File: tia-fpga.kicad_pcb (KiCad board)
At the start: 2 copper layers, 76 x 36 mm, 28 parts, among them J1 PinSocket_1x24_P2.54mm_Vertic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, J2 PinHeader_1x20_P2.54mm_Vertic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, J3 PinHeader_1x20_P2.54mm_Vertic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, J4 PinSocket_1x24_P2.54mm_Vertic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, U1 SOIC-14_3.9x8.7mm_P1.27mm, U2 SOIC-20W_7.5x12.8mm_P1.27mm, U3 SOIC-20W_7.5x12.8mm_P1.27mm, U4 SOIC-20W_7.5x12.8mm_P1.27mm, U5 SOT-23-5

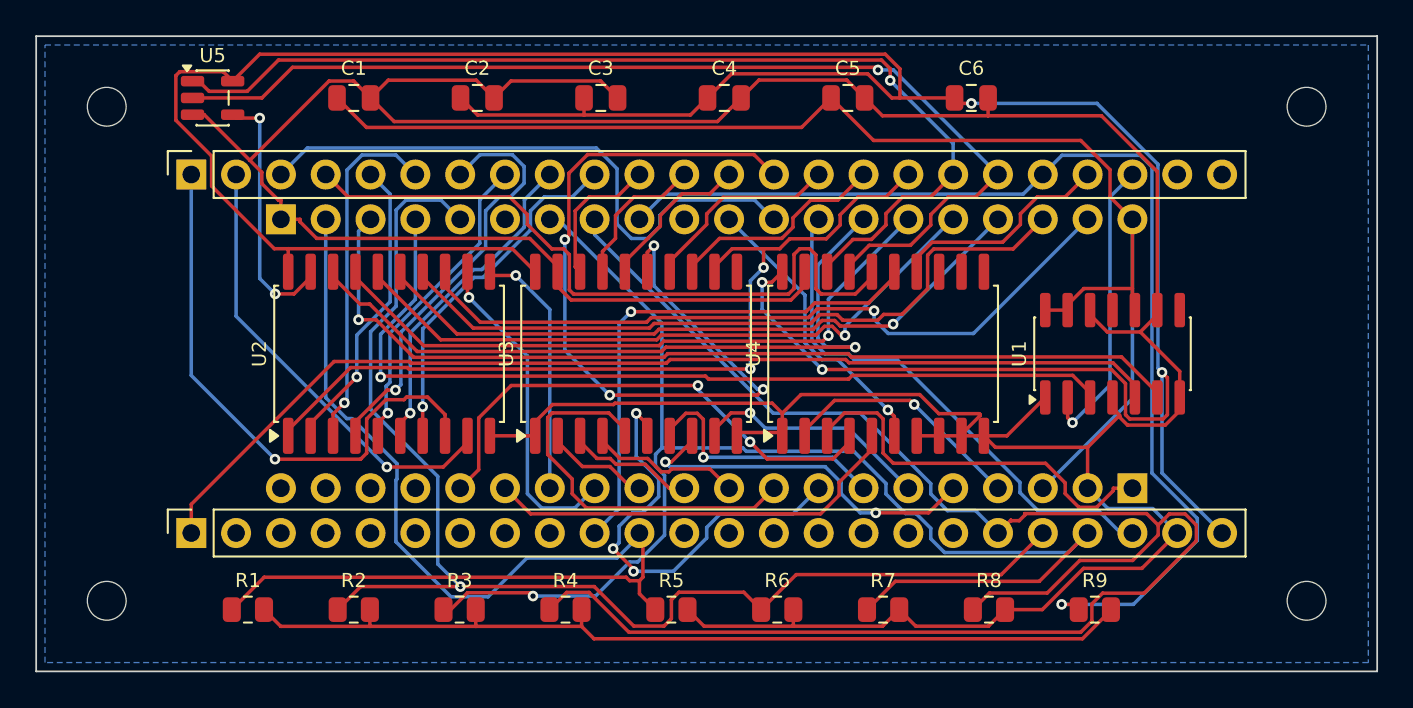
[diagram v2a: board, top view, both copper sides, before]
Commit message: Solve the pin assignment and reorder the buffers; drop the mounting holes
The buses crossed the board because the FPGA signals were assigned to
header positions in listing order. But which GPIO carries which signal is
free - the Tang Nano's header-to-package map is fixed, nothing says F_D0
has to sit on header pin 5. So it is now solved rather than listed:
Hungarian assignment over the 29 usable positions, minimising the
distance from each FPGA pin to the TIA pin it serves.

Summed |x_header - x_TIA| goes from 737 mm to 127 mm, with several
signals landing at exactly the same x as their target. The buffers are
then ordered by the centroid of what each carries: U1, U4, U3, U2.

Together:

  segments  758 -> 601
  vias       47 -> 31
  copper   2.19 -> 1.68 m

Mounting holes dropped. They were only ever going to hold the board to
something that does not exist inside a 2600 - it hangs from its own pins
in the TIA socket - and they had pushed the outline out to 76 x 36 mm.
Back to 70 x 32.

Silkscreen references moved beside the passives rather than above them;
in a 5 mm margin, above means into the board edge. That took the
silkscreen violations from 11 to 1.

Routing needed 0.18 mm track on top of the 0.13 mm clearance to close.
Worth recording how brittle this is: moving U5 by half a millimetre to
clear a courtyard warning cost two unrouted connections and a worse
score, because Freerouting is deterministic per input and any change
reshuffles everything. U5 went back where it was.

DRC: 0 clearance, 0 unconnected, 0 shorts. Two notes remain, both checked
by hand - one silk mark over copper, and the U5/J1 courtyard overlap
where the copper actually clears by 1.24 mm.

fpga/tia_fpga.cst carries the solved assignment and says not to reshuffle
it casually, since the layout depends on it.

Co-Authored-By: Claude Opus 5 <noreply@anthropic.com>
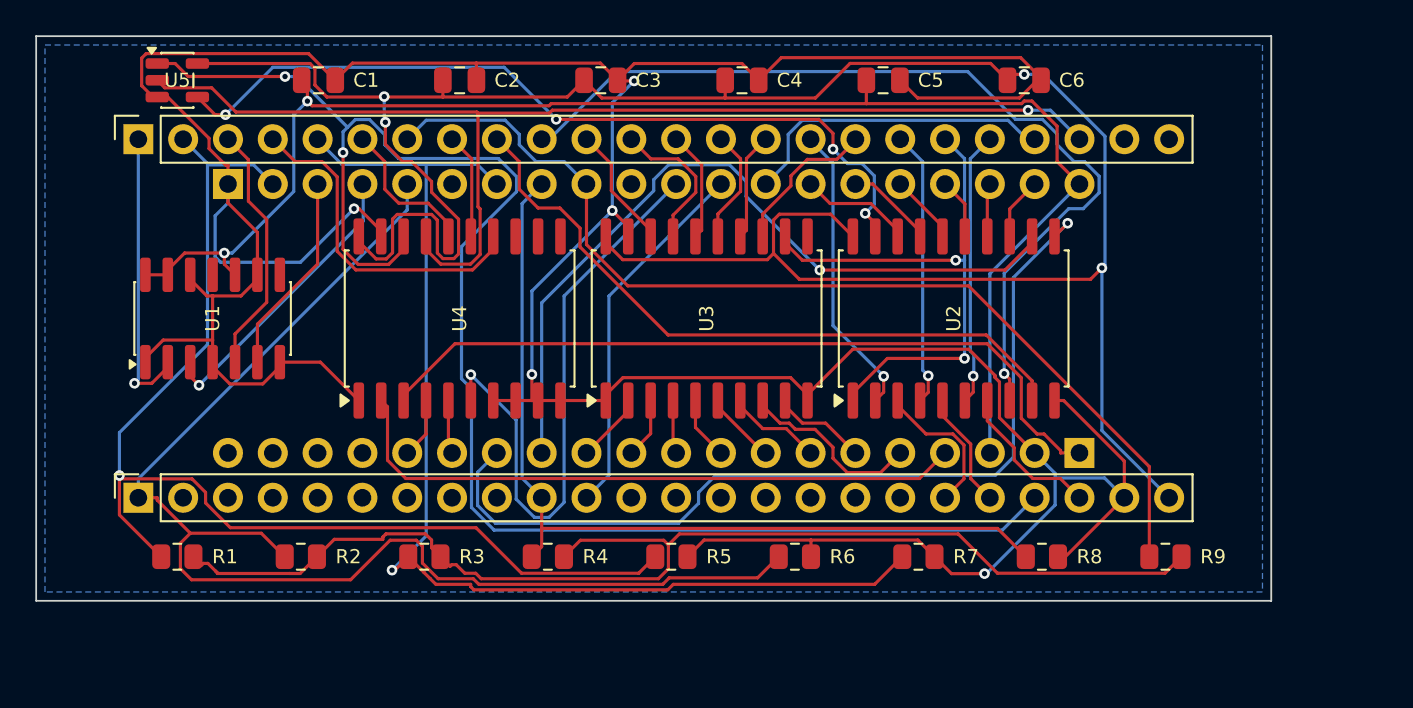
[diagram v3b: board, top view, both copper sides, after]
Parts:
- removed H1, H2, H3, H4: MountingHole_2.2mm_M2, MountingHole_2.2mm_M2
- moved U1 51.0 mm to (10.0, 16.0)
- moved U2 32.1 mm to (52.0, 16.0)
- moved U4 24.1 mm to (24.0, 16.0)
- moved R1 5.00 mm to (8.00, 29.5)
- moved R9 5.00 mm to (64.0, 29.5)
- moved U3 4.47 mm to (38.0, 16.0)
- moved R2 4.24 mm to (15.0, 29.5)
- moved R8 4.24 mm to (57.0, 29.5)
- moved J2 3.61 mm to (10.9, 8.38)
- moved J3 3.61 mm to (59.1, 23.6)
- moved R3 3.61 mm to (22.0, 29.5)
- moved R7 3.61 mm to (50.0, 29.5)
- moved J1 3.61 mm to (5.79, 5.84)
- moved J4 3.61 mm to (5.79, 26.2)
- moved C6 3.16 mm to (56.0, 2.50)
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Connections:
- J1 pad 1: /F_D6 -> /F_PHI0
- J1 pad 10: /F_D5 -> /F_D6
- J1 pad 16: /F_A5 -> /F_D0
- J1 pad 17: /F_RW -> /F_A5
- J1 pad 18: /F_CS0_N -> /F_D2
- J1 pad 19: /F_CS3_N -> /F_RW
- J1 pad 2: /F_D7 -> /F_CSYNC
- J1 pad 20: /F_COL -> /F_D4
- J1 pad 21: /F_OSC -> /F_AU0
- J1 pad 22: /F_PHI0 -> /F_CS3_N
- J1 pad 3: /F_AU1 -> /F_RDY
- J1 pad 4: /F_I4 -> /F_OSC
- J1 pad 5: /F_D0 -> /F_LUM2
- J1 pad 6: /F_D1 -> /F_I4
- J1 pad 7: /F_D2 -> /F_COL
- J1 pad 8: /F_D3 -> /F_I5
- J1 pad 9: /F_D4 -> /F_D7
- J4 pad 1: /F_RDY -> /F_LUM1
- J4 pad 10: /F_I5 -> /F_LUM0
- J4 pad 11: /F_CSYNC -> /F_AU1
- J4 pad 19: /F_LUM0 -> /F_D1
- J4 pad 20: /F_LUM1 -> /F_D3
- J4 pad 21: /F_LUM2 -> /F_CS0_N
- J4 pad 22: /F_AU0 -> /F_D5
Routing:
- net /F_LUM0: track 98.1 -> 50.4 mm
- net /F_RDY: track 59.9 -> 14.3 mm
- net /TIA_RDY: track 53.4 -> 11.5 mm, vias 1 -> 0
- net /F_A3: track 47.6 -> 6.50 mm, vias 4 -> 0
- net /TIA_D5: track 42.0 -> 3.56 mm, vias 1 -> 0
- net /TIA_D4: track 40.6 -> 3.03 mm
- net /TIA_D7: track 14.4 -> 51.7 mm
- net /TIA_D0: track 41.9 -> 6.37 mm, vias 1 -> 0
- net /TIA_D3: track 38.5 -> 3.44 mm, vias 1 -> 0
- net /TIA_PHI0: track 50.8 -> 16.8 mm
- net /TIA_D2: track 37.9 -> 3.96 mm, vias 1 -> 0
- net /TIA_D1: track 37.4 -> 5.06 mm, vias 1 -> 0
- net /DBUS_OE_N: track 14.7 -> 46.8 mm, vias 2 -> 4
- net +3V3: track 171.3 -> 139.2 mm
- net /F_I4: track 40.4 -> 8.51 mm
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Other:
- board size 76 x 36 mm -> 70 x 32 mm

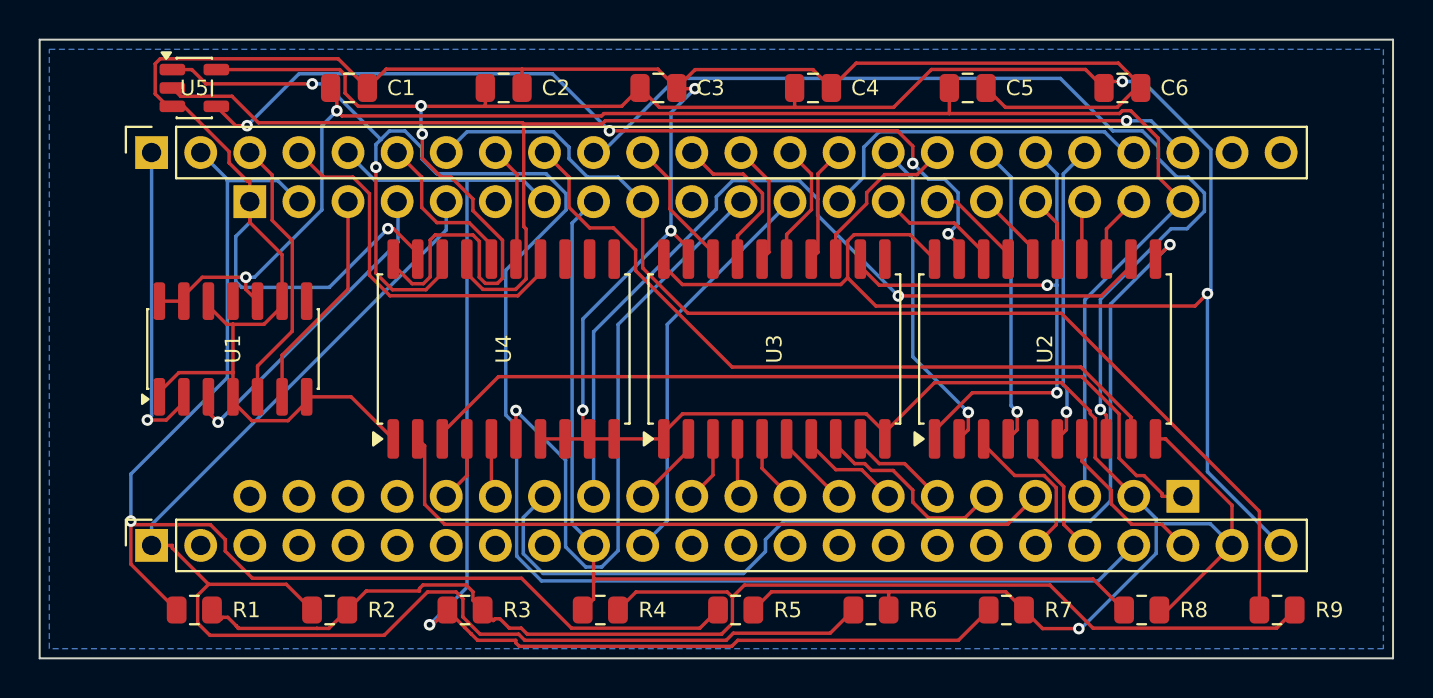
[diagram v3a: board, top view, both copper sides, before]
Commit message: Respin the board as rev B: open-drain pads and BLK
Every TIA video and sound pad is open drain on the die, and the console's
pull-ups and summing network are built around that. Rev B puts SYNC,
LUM0-2, COL, BLK, AUD0 and AUD1 through four 74LVC2G07 (U6-U9, SOT-23-6,
5 V tolerant open-drain outputs) in the top margin above J2, with 100 nF
C7-C10 beside them. Their designators are on the back silkscreen, since
the front has no room left.

BLK (pin 6) is now driven. The original 2600 and the 2600A rev 16 feed it
into the chroma node, which holds the colour burst down during blanking.
The FPGA pin for it comes from reading /CS0 OR /CS3 straight off U5 (net
F_CS_N, the signal that already enables U2) instead of both selects;
tia_board.v ties the core's cs3_n low.

R1-R9 are gone. They copied the console's own video DAC and summing
network, which a board in the TIA socket must not duplicate. C1-C6 moved
to the bottom margin. F_OSC moved to pin 63 (RPLL_T_in, J6/1), so the
colour clock reaches the PLL on its dedicated input and PR1014 is gone.

The FPGA pin assignment was solved again against the pads each net really
reaches (Hungarian assignment, 378 mm summed). Freerouting 2.2.4 routed it
in 557 segments, 29 vias and 1.29 m of copper (rev A: 601, 31, 1.68 m).
One GND connection at C10 was closed by hand, with a via inside the main
pour. ERC 0; DRC 0 violations, 0 unconnected pads. The gerbers, drill
file, PDFs, BOMs and renders are regenerated. The rev A PDFs are removed,
since rev A was never built.

Timing: hblank_next now comes from the horizontal counter's level decodes
(shb_next, rhb_next) instead of the H@2 pulses. That keeps the phase
divider out of the object clock enables. shb_next also carries RSYNC's
countdown: a restart can land on HMOVE's grid, and the decodes alone
would merge a pulse there although HBLANK comes on at that very half
clock. No trace covers the case, so random runs of HMOVE, RSYNC and HMxx
writes checked hblank_next against HBLANK one clock l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
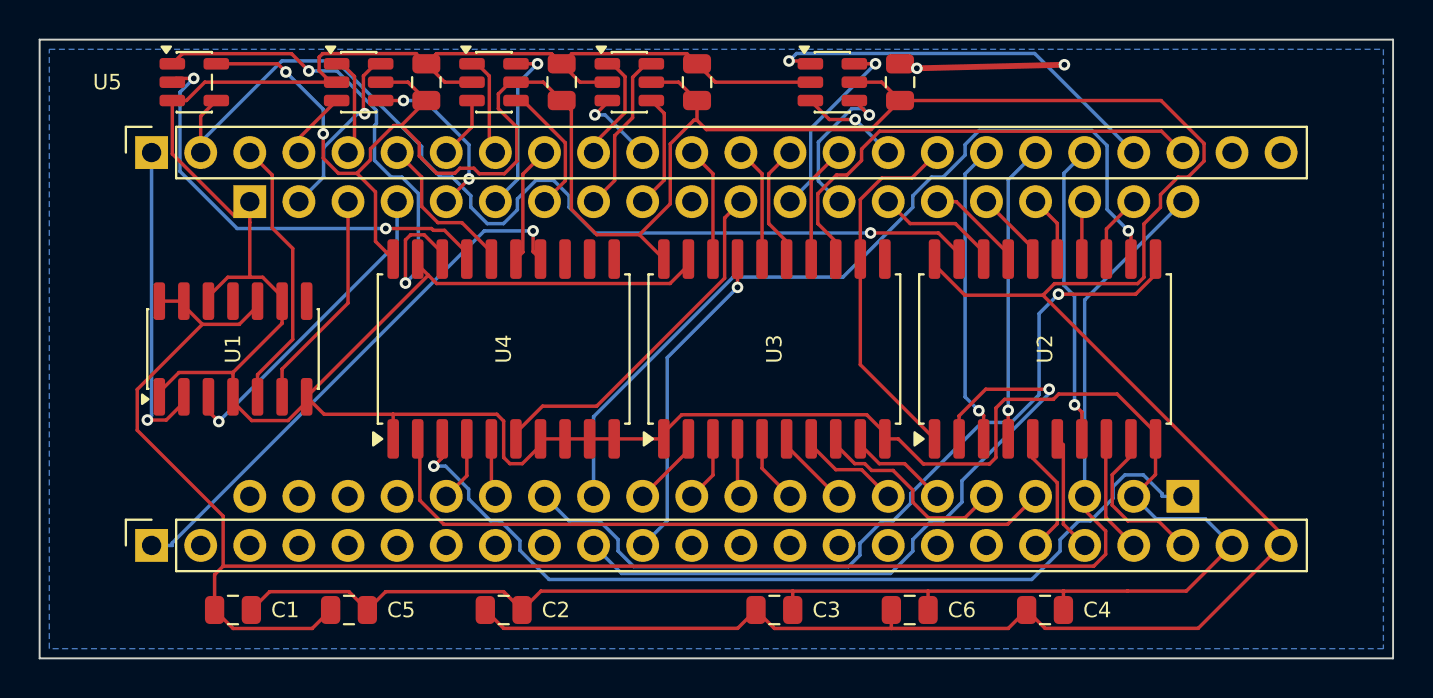
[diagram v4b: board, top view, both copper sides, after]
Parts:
- removed R1, R2, R3, R4, R5, R6, R7, R8, R9: R_0805_2012Metric, R_0805_2012Metric
- added C10: 100n, C_0805_2012Metric, F.Cu at (44.5, 2.20)
- added C7: 100n, C_0805_2012Metric, F.Cu at (20.0, 2.20)
- added C8: 100n, C_0805_2012Metric, F.Cu at (27.0, 2.20)
- added C9: 100n, C_0805_2012Metric, F.Cu at (34.0, 2.20)
- added U6: 74LVC2G07, SOT-23-6, F.Cu at (16.5, 2.20)
- added U7: 74LVC2G07, SOT-23-6, F.Cu at (23.5, 2.20)
- added U8: 74LVC2G07, SOT-23-6, F.Cu at (30.5, 2.20)
- added U9: 74LVC2G07, SOT-23-6, F.Cu at (41.0, 2.20)
- moved C5 41.9 mm to (16.0, 29.5)
- moved C4 29.5 mm to (52.0, 29.5)
- moved C6 29.2 mm to (45.0, 29.5)
- moved C1 27.7 mm to (10.0, 29.5)
- moved C3 27.7 mm to (38.0, 29.5)
- moved C2 27.0 mm to (24.0, 29.5)
- moved U5 0.30 mm to (8.00, 2.20)
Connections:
- J1 pad 10: /F_D6 -> /F_LUM0
- J1 pad 11: /F_A0 -> /F_COL
- J1 pad 12: /F_A1 -> /F_A0
- J1 pad 16: /F_D0 -> /F_AU0
- J1 pad 17: /F_A5 -> /F_RW
- J1 pad 18: /F_D2 -> /F_D1
- J1 pad 19: /F_RW -> /F_D2
- J1 pad 2: /F_CSYNC -> /F_CS_N
- J1 pad 20: /F_D4 -> /F_D5
- J1 pad 21: /F_AU0 -> /F_AU1
- J1 pad 22: /F_CS3_N -> /F_A5
- J1 pad 4: /F_OSC -> /F_LUM1
- J1 pad 5: /F_LUM2 -> /F_CSYNC
- J1 pad 7: /F_COL -> /F_LUM2
- J1 pad 8: /F_I5 -> /F_BLK
- J1 pad 9: /F_D7 -> /F_I5
- J2 pad 12: /F_AU1 -> /TIA_AU1
- J2 pad 13: /F_AU0 -> /TIA_AU0
- J2 pad 2: /F_CSYNC -> /TIA_CSYNC
- J2 pad 5: /F_LUM1 -> /TIA_LUM1
- J2 pad 6: unconnected-(J2-Pin_6-Pad6) -> /TIA_BLK
- J2 pad 7: /F_LUM2 -> /TIA_LUM2
- J2 pad 8: /F_LUM0 -> /TIA_LUM0
- J2 pad 9: /F_COL -> /TIA_COL
- J4 pad 1: /F_LUM1 -> /F_OSC
- J4 pad 10: /F_LUM0 -> /F_D0
- J4 pad 11: /F_AU1 -> /F_A1
- J4 pad 19: /F_D1 -> /F_D3
- J4 pad 20: /F_D3 -> /F_D4
- J4 pad 21: /F_CS0_N -> /F_D6
- J4 pad 22: /F_D5 -> /F_D7
- U2 pad 19: /DBUS_OE_N -> /F_CS_N
- U5 pad 4: /DBUS_OE_N -> /F_CS_N
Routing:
- net /F_LUM1: track 73.4 -> 3.50 mm
- net /VIDEO_SUM: track 68.5 -> 0.00 mm
- net /F_LUM2: track 65.9 -> 3.24 mm, vias 1 -> 0
- net /F_CS0_N: track 89.1 -> 27.5 mm
- net /F_CSYNC: track 64.8 -> 5.27 mm, vias 1 -> 0
- net /F_COL: track 58.1 -> 4.29 mm, vias 0 -> 1
- net /F_CS_N: track 0.00 -> 52.2 mm, vias 0 -> 1
- net /DBUS_OE_N: track 46.8 -> 0.00 mm, vias 4 -> 0
- net /F_D6: track 51.5 -> 6.12 mm, vias 1 -> 0
- net /F_LUM0: track 50.4 -> 5.79 mm
- net /F_CS3_N: track 66.2 -> 23.2 mm, vias 1 -> 2
- net +3V3: track 139.2 -> 178.2 mm, vias 4 -> 2
- net /F_D7: track 38.7 -> 8.35 mm
- net /F_D0: track 16.7 -> 35.7 mm
- net /F_A5: track 8.66 -> 24.8 mm
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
